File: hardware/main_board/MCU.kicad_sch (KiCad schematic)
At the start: 17 parts, among them IC1 M0G3507QDGS32RQ1, J1 Conn_01x06_Pin, J8 2x5 Socket Pins, SW1 RST, U3 LP-MSPM0G3507

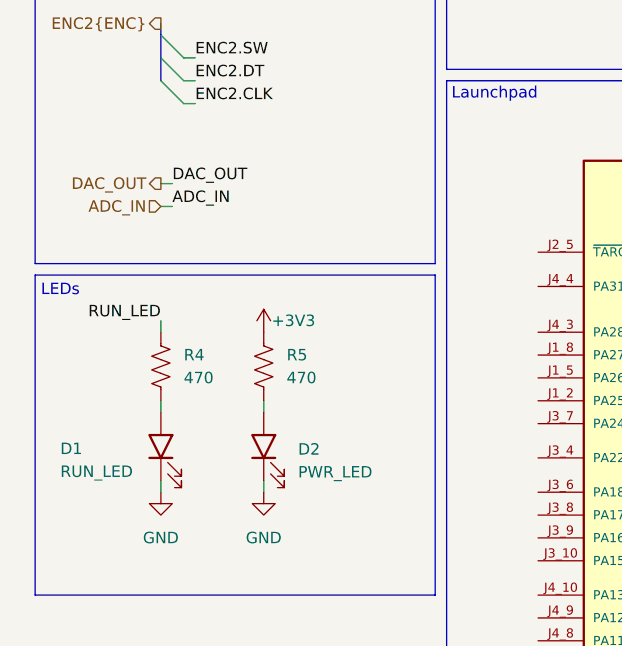
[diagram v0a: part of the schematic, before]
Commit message: fixed peripheral board dimensions to be compatible with 2.54 mm pitch protoboard for daisy chaining. deleted gerbers. added some more content to main board (wip)
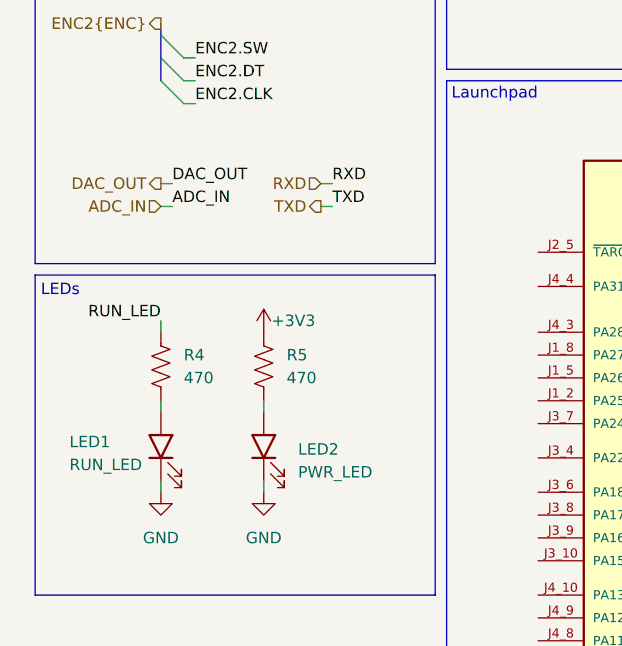
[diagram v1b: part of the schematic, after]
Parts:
- removed D1: RUN_LED, 445L:LED_D5.0mm, symbol ECE445L:LED
- removed D2: PWR_LED, 445L:LED_D5.0mm, symbol ECE445L:LED
- added LED1: RUN_LED, SamacSys_Parts:LEDC2012X40N, symbol ECE445L:LED
- added LED2: PWR_LED, SamacSys_Parts:LEDC2012X40N, symbol ECE445L:LED
- J8: footprint Connector_PinSocket_2.54mm:PinSocket_2x05_P2.54mm_Vertical -> SamacSys_Parts:logic_analyzer_slot_2x5_2.54mm
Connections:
- net GND: now also LED1.1 (K), LED2.1 (K)
- net at R5.2: now also LED2.2 (A)
- net at R4.2: now also LED1.2 (A)
